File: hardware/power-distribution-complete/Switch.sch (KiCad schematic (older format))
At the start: 63 parts, among them J10 Parallell, J11 Parallell, J12 Parallell, J13 Parallell, J14 Parallell, J15 Parallell, J16 Parallell, J17 Parallell, J3 Parallell, J4 Parallell, J5 Parallell, J6 Parallell, J7 Parallell, J8 Parallell, J9 Parallell, Q1 Q_PMOS_GDS, Q10 Q_PMOS_GDS, Q11 Q_PMOS_GDS, Q12 Q_PMOS_GDS, Q13 Q_PMOS_GDS, Q14 Q_PMOS_GDS, Q15 Q_PMOS_GDS, Q16 Q_PMOS_GDS, Q2 Q_PMOS_GDS, Q3 Q_PMOS_GDS, Q4 Q_PMOS_GDS, Q5 Q_PMOS_GDS, Q6 Q_PMOS_GDS, Q7 Q_PMOS_GDS, Q8 Q_PMOS_GDS, Q9 Q_PMOS_GDS

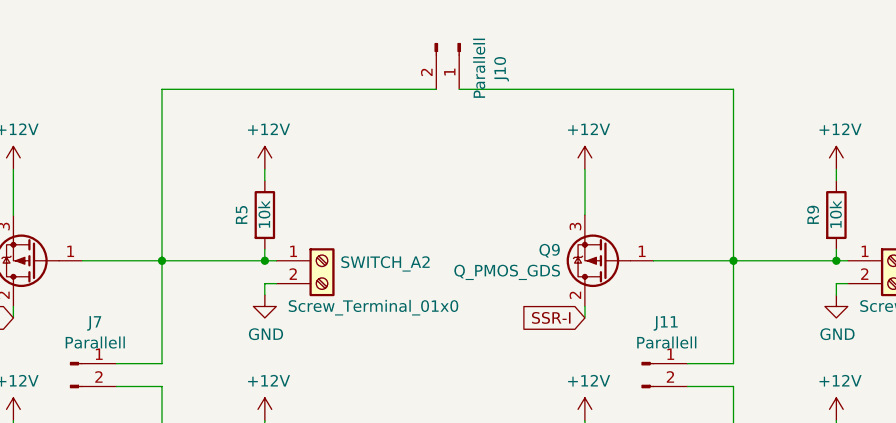
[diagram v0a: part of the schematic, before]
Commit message: Updated the power distribution schematic and pcb
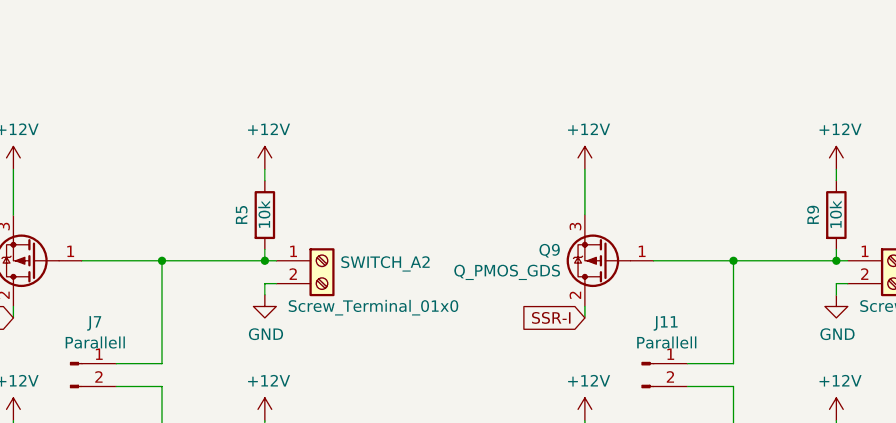
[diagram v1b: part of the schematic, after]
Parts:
- removed J10: Parallell, Connector_PinHeader_2.54mm:PinHeader_1x02_P2.54mm_Vertical, symbol Connector:Conn_01x02_Male
- Q1, Q10, Q11, Q12, Q13, Q14, Q15, Q16, Q2, Q3, Q4, Q5, Q6, Q7, Q8, Q9: footprint Package_TO_SOT_SMD:TO-252-2 -> mosfet:TO-252-2-ThermalVias
- SWITCH_A1, SWITCH_A2, SWITCH_A3, SWITCH_A4, SWITCH_B1, SWITCH_B2, SWITCH_B3, SWITCH_B4, SWITCH_C1, SWITCH_C2, SWITCH_C3, SWITCH_C4, SWITCH_C5, SWITCH_C6, SWITCH_C7, SWITCH_C8: footprint TerminalBlock_Phoenix:TerminalBlock_Phoenix_PT-1,5-2-5.0-H_1x02_P5.00mm_Horizontal -> connectors:TerminalBlock_02_P5.00mm
